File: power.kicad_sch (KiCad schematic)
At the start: 27 parts, among them J12 Power Connector, Q7 AO3404A, Q8 AO3407A, U1 LM78L05_TO92, U2 TL074, U3 TL074, U4 TL074

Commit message: power
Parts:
- C7, C8: footprint Capacitor_THT:C_Disc_D4.3mm_W1.9mm_P5.00mm -> Capacitor_SMD:C_1206_3216Metric_Pad1.33x1.80mm_HandSolder
- R23: footprint Resistor_THT:R_Axial_DIN0207_L6.3mm_D2.5mm_P2.54mm_Vertical -> Resistor_SMD:R_1206_3216Metric_Pad1.30x1.75mm_HandSolder
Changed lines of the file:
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@@
 			)
 		)
-		(property "Footprint" "Resistor_THT:R_Axial_DIN0207_L6.3mm_D2.5mm_P2.54mm_Vertical"
+		(property "Footprint" "Resistor_SMD:R_1206_3216Metric_Pad1.30x1.75mm_HandSolder"
 			(at 116.84 154.178 90)
 			(effects
@@
 			)
 		)
-		(property "Footprint" "Capacitor_THT:C_Disc_D4.3mm_W1.9mm_P5.00mm"
+		(property "Footprint" "Capacitor_SMD:C_1206_3216Metric_Pad1.33x1.80mm_HandSolder"
 			(at 64.4652 177.8 0)
 			(effects
@@
 			)
 		)
-		(property "Footprint" "Capacitor_THT:C_Disc_D4.3mm_W1.9mm_P5.00mm"
+		(property "Footprint" "Capacitor_SMD:C_1206_3216Metric_Pad1.33x1.80mm_HandSolder"
 			(at 116.5352 177.8 0)
 			(effects

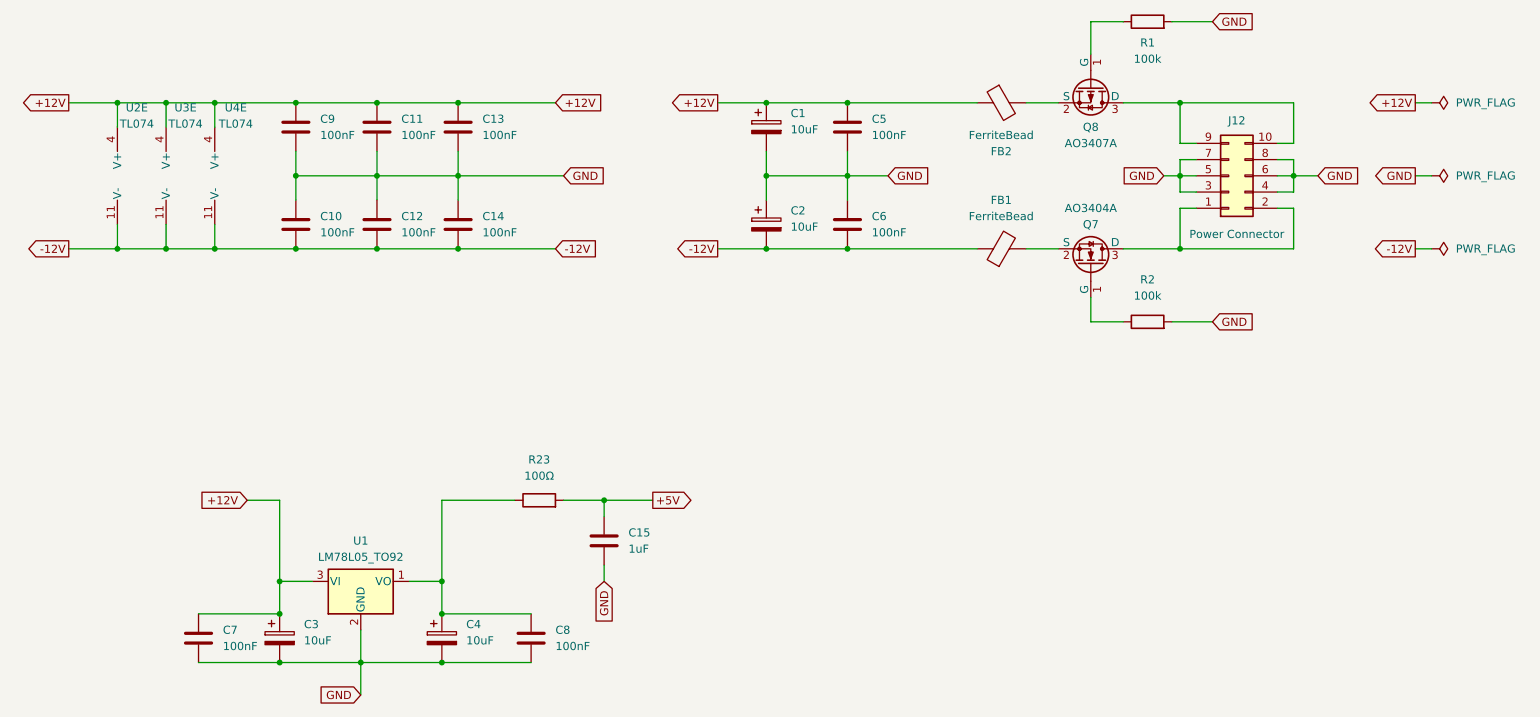
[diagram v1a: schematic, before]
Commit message: Updated control panel
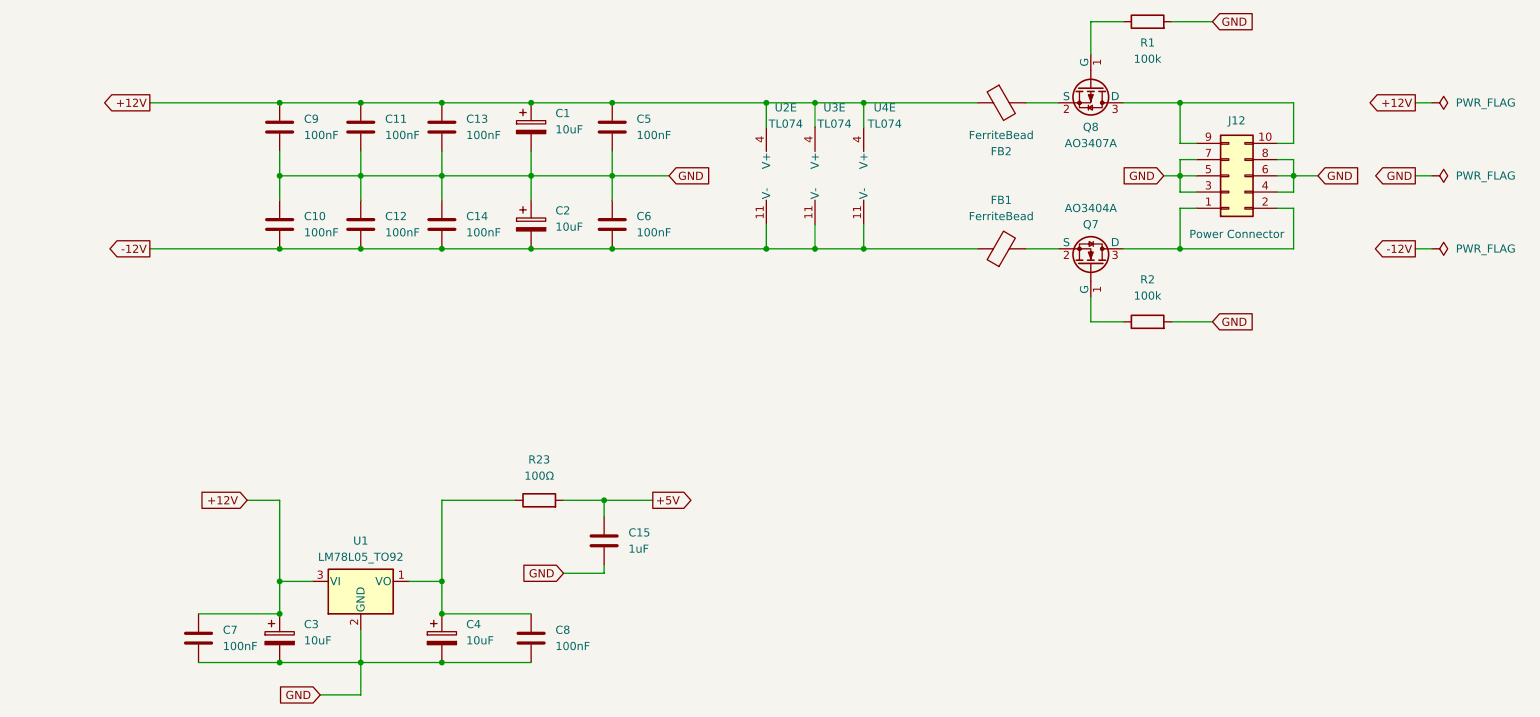
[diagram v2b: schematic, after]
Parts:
- C10, C11, C12, C13, C14, C5, C6, C9: footprint Capacitor_SMD:C_1206_3216Metric -> Capacitor_SMD:C_1206_3216Metric_Pad1.33x1.80mm_HandSolder
- C15: value 1uF_Radial_TH -> 1uF
- R1, R2: footprint Resistor_SMD:R_1206_3216Metric -> Resistor_SMD:R_1206_3216Metric_Pad1.30x1.75mm_HandSolder
- R23: value 100Ω_TH0.125 -> 100
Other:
- moved on the sheet: C1, C10, C11, C12, C13, C14, C2, C5, C6, C9

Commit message: Added test point
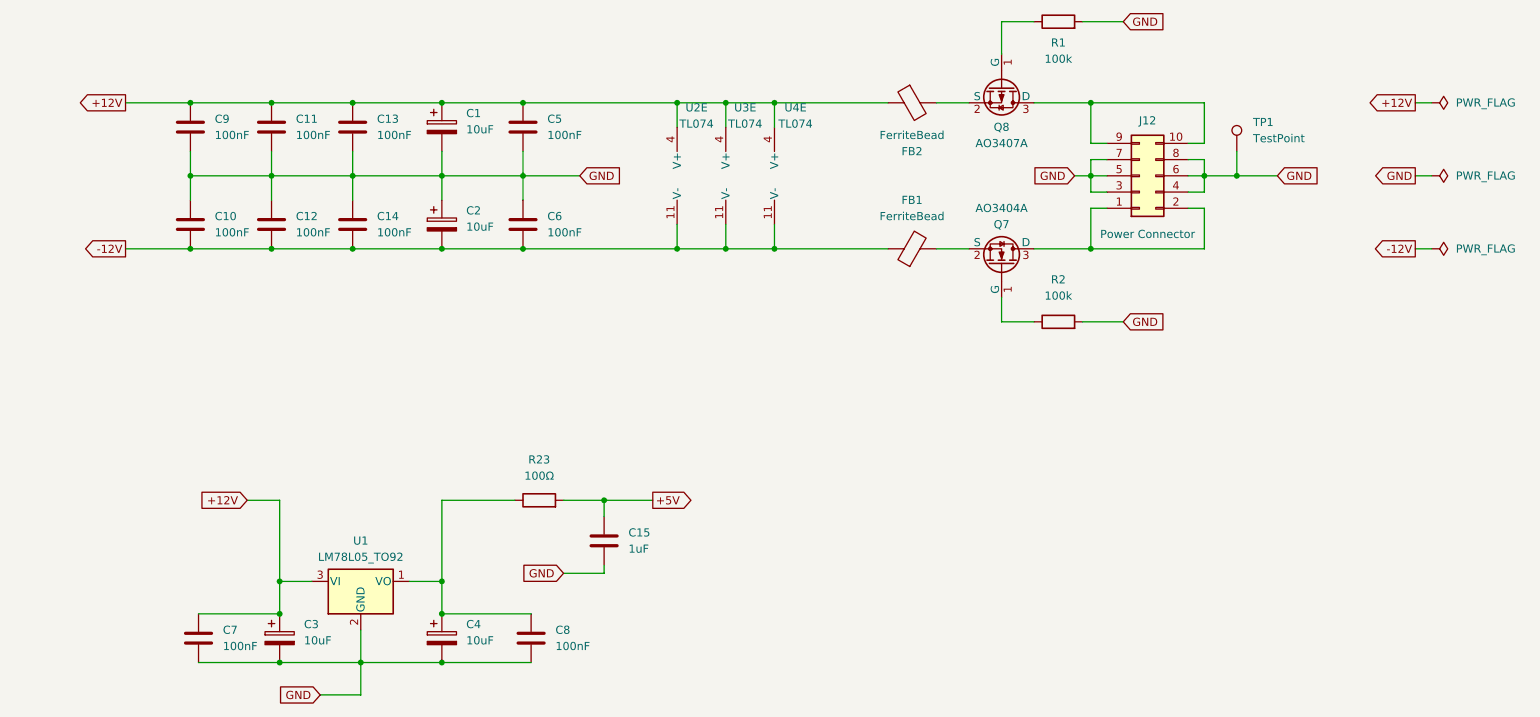
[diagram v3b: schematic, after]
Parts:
- added TP1: TestPoint, TestPoint:TestPoint_THTPad_2.0x2.0mm_Drill1.0mm, symbol Connector:TestPoint
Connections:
- net GND: now also TP1.1
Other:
- moved on the sheet: C1, C10, C11, C12, C13, C14, C2, C5, C6, C9, FB1, FB2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

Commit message: Updated power tracing
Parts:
- C1: footprint Capacitor_THT:CP_Radial_D5.0mm_P2.00mm -> Capacitor_SMD:CP_Elec_5x5.8; Mouser (none) -> https://eu.mouser.com/ProductDetail/Panasonic/EEH-ZA1H100R?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
- C2: footprint Capacitor_THT:CP_Radial_D5.0mm_P2.00mm -> Capacitor_SMD:CP_Elec_5x5.8
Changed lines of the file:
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@@
 			)
 		)
-		(property "Footprint" "Capacitor_THT:CP_Radial_D5.0mm_P2.00mm"
+		(property "Footprint" "Capacitor_SMD:CP_Elec_5x5.8"
 			(at 102.5652 97.79 0)
 			(hide yes)
@@
 			)
 		)
-		(property "Datasheet" ""
+		(property "Datasheet" "https://industrial.panasonic.com/cdbs/www-data/pdf/RDD0000/ABA0000C1221.pdf"
 			(at 101.6 93.98 0)
 			(hide yes)
@@
 			)
 		)
-		(property "Description" "Panasonic EEUFC1H100L"
+		(property "Description" "Panasonic EEH-ZA1H100R"
+			(at 101.6 93.98 0)
+			(hide yes)
+			(show_name no)
+			(do_not_autoplace no)
+			(effects
+				(font
+					(size 1.27 1.27)
+				)
+			)
+		)
+		(property "Mouser" "https://eu.mouser.com/ProductDetail/Panasonic/EEH-ZA1H100R?qs=7UCyOFMWVHYLkHnrAgGq6g%3D%3D"
 			(at 101.6 93.98 0)
 			(hide yes)
@@
 			)
 		)
-		(property "Footprint" "Capacitor_THT:CP_Radial_D5.0mm_P2.00mm"
+		(property "Footprint" "Capacitor_SMD:CP_Elec_5x5.8"
 			(at 102.5652 113.03 0)
 			(hide yes)
@@
 			)
 		)
-		(property "Datasheet" ""
+		(property "Datasheet" "https://industrial.panasonic.com/cdbs/www-data/pdf/RDD0000/ABA0000C1221.pdf"
 			(at 101.6 109.22 0)
 			(hide yes)
@@
 			)
 		)
-		(property "Description" "Panasonic EEUFC1H100L"
+		(property "Description" "Panasonic EEH-ZA1H100R"
 			(at 101.6 109.22 0)
 			(hide yes)

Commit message: save chages
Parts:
- added C16: 100nF, Capacitor_SMD:C_1206_3216Metric_Pad1.33x1.80mm_HandSolder, symbol Device:C
- added F1, F2: Polyfuse, Fuse:Fuse_1206_3216Metric_Pad1.42x1.75mm_HandSolder, symbol Device:Polyfuse
- added R24: 3.3k, Resistor_SMD:R_1206_3216Metric_Pad1.30x1.75mm_HandSolder, symbol Device:R
- added U5: LM4040DBZ-5, Package_TO_SOT_SMD:SOT-23_Handsoldering, symbol Reference_Voltage:LM4040DBZ-5
- C1: value 10uF -> 22uF, 25V; Mouser https://eu.mouser.com/ProductDetail/Panasonic/EEH-ZA1H100R?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 -> (none)
- C2: value 10uF -> 22uF, 25V
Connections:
- net +12V: now also R24.1
- net GND: now also C16.2
- net at J12.10 (+12V), J12.9 (+12V): now also F1.1; no longer Q8.3 (D)
- net at J12.1 (-12V), J12.2 (-12V): now also F2.1; no longer Q7.3 (D)
- new net: F1.2, Q8.3 (D)
- new net: C16.1, R24.2, U5.2 (A)
- new net: F2.2, Q7.3 (D)
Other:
- moved on the sheet: C10, C11, C12, C13, C14, C9, J12, TP1

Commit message: save changes
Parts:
- removed C15: 1uF, Capacitor_THT:C_Rect_L7.2mm_W4.5mm_P5.00mm_FKS2_FKP2_MKS2_MKP2, symbol Device:C
- removed C3, C4: 10uF, Capacitor_THT:CP_Radial_D5.0mm_P2.00mm, symbol Device:C_Polarized
- removed C7, C8: 100nF, Capacitor_SMD:C_1206_3216Metric_Pad1.33x1.80mm_HandSolder, symbol Device:C
- removed R23: 100, Resistor_SMD:R_1206_3216Metric_Pad1.30x1.75mm_HandSolder, symbol Device:R
- removed U1: LM78L05_TO92, Package_TO_SOT_THT:TO-92_Inline_Wide, symbol Regulator_Linear:LM78L05_TO92
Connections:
- net +5V: now also U5.1 (K)
